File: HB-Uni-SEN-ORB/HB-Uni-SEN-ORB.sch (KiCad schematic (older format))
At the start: 27 parts, among them J2 BNC, U1 Arduino_Pro_Mini, U2 CC1101, U3 LM2660M, U4 LM358M_NOPB

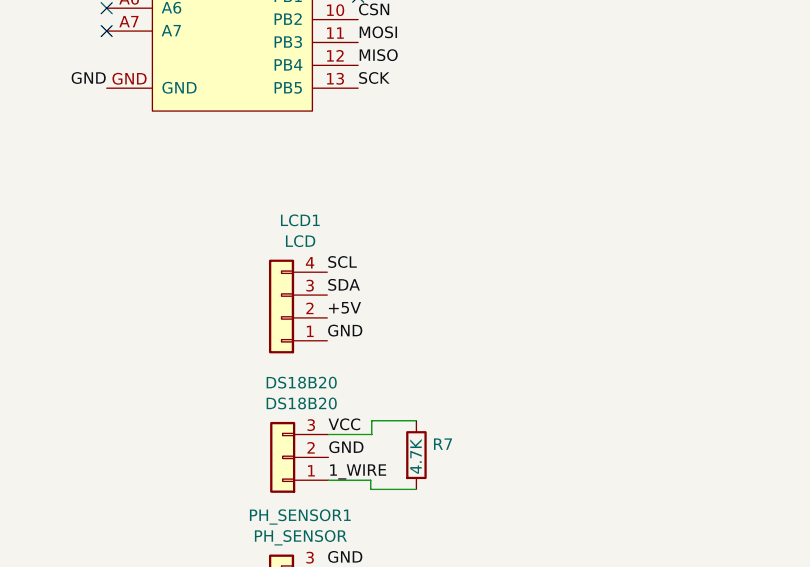
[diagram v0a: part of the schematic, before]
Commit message: Add files via upload
Add I2C Pullup
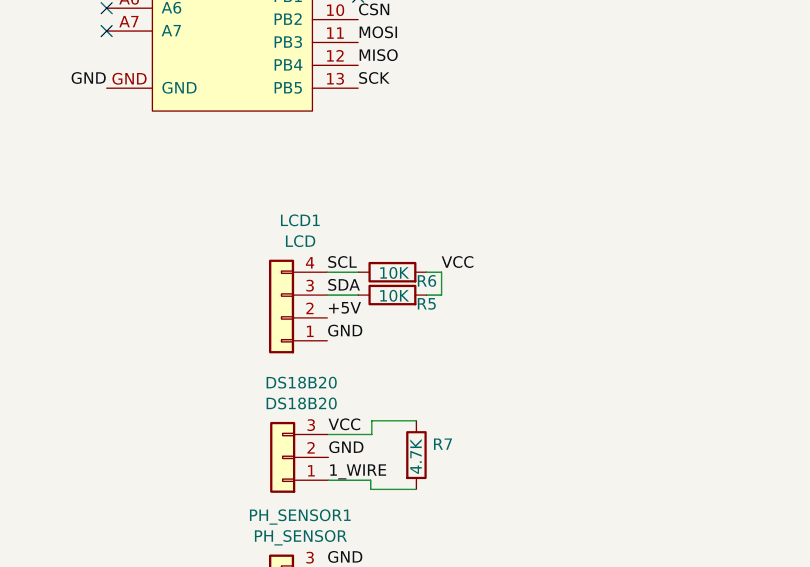
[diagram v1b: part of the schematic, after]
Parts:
- added R5, R6: 10K, Resistor_SMD:R_0805_2012Metric_Pad1.20x1.40mm_HandSolder, symbol Device:R
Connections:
- net SCL: now also R6.1
- net SDA: now also R5.1
- net VCC: now also R5.2, R6.2
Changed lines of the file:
@@
 Text Label 5965 4785 0    50   ~ 0
 GND
+$Comp
+L Device:R R6
+U 1 1 608629BB
+P 6250 3495
+F 0 "R6" V 6210 3345 50  0000 C CNN
+F 1 "10K" V 6245 3490 50  0000 C CNN
+F 2 "Resistor_SMD:R_0805_2012Metric_Pad1.20x1.40mm_HandSolder" V 6180 3495 50  0001 C CNN
+F 3 "~" H 6250 3495 50  0001 C CNN
+	1    6250 3495
+	0    -1   -1   0
+$EndComp
+$Comp
+L Device:R R5
+U 1 1 6086540B
+P 6250 3595
+F 0 "R5" V 6210 3445 50  0000 C CNN
+F 1 "10K" V 6245 3590 50  0000 C CNN
+F 2 "Resistor_SMD:R_0805_2012Metric_Pad1.20x1.40mm_HandSolder" V 6180 3595 50  0001 C CNN
+F 3 "~" H 6250 3595 50  0001 C CNN
+	1    6250 3595
+	0    -1   -1   0
+$EndComp
+Wire Wire Line
+	5965 3495 6100 3495
+Wire Wire Line
+	5965 3595 6100 3595
+Wire Wire Line
+	6400 3495 6465 3495
+Wire Wire Line
+	6465 3495 6465 3595
+Wire Wire Line
+	6465 3595 6400 3595
+Text Label 6465 3495 0    50   ~ 0
+VCC
 $EndSCHEMATC
